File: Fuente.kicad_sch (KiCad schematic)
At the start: 0 parts

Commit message: Avance
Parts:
- added C1: 100nF/400VAC, Capacitor_THT:C_Disc_D10.5mm_W5.0mm_P7.50mm, symbol Device:C
- added C1, C6: 100nF/50v, 1-Capacitor:C_0805_2012Metric, symbol Device:C
- added C2: 220uF/25v, Capacitor_THT:CP_Radial_D8.0mm_P3.50mm, symbol Device:C_Polarized
- added C3, C4: 1uF/50v, 1-Capacitor:C_1206_3216Metric, symbol 1-Capacitor:C_1206
- added C38, C60: 10uF/16V, Capacitor_THT:CP_Radial_D5.0mm_P2.50mm, symbol Device:C_Polarized
- added C59, C61: 1uF 50V, 1-Capacitor:C_1206_3216Metric, symbol 1-Capacitor:C_0805
- added F1: 250VAC 0.5AAC, Fuse:Fuseholder_TR5_Littelfuse_No560_No460, symbol Device:Fuse
- added J8: Screw_Terminal_01x02, 1-Terminal-Block:DG126_5.0_02P, symbol 1-Terminal-Block:DG126_5.0_02P
- added PS2: IRM-10-24, Converter_ACDC:Converter_ACDC_MeanWell_IRM-10-xx_THT, symbol Converter_ACDC:IRM-10-24
- added RV1: 10D561K, Varistor:RV_Disc_D12mm_W3.9mm_P7.5mm, symbol Device:Varistor
- added U4, U6: LD29150, Package_TO_SOT_SMD:TO-252-2, symbol LIB_SCH_CONTR:LD29150
- added U5: L78M08CDT-TR, Package_TO_SOT_SMD:TO-252-2, symbol Regulator_Linear:uA7810
- added U7: OKI-78SR-12_1.0-W36-C, Converter_DCDC:Converter_DCDC_Murata_OKI-78SR_Vertical, symbol Converter_DCDC:OKI-78SR-12_1.0-W36-C
- added U8: uA7810, Package_TO_SOT_SMD:TO-263-3_TabPin2, symbol Regulator_Linear:uA7810
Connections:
- new net: F1.1, J8.1 (Pin_1)
- new net: C1.1, F1.2, PS2.2 (AC/L), RV1.1
- new net: C1.2, J8.2 (Pin_2), PS2.1 (AC/N), RV1.2
- new net 10V: C6.1, U8.3 (OUT)
- new net 12V: C3.1, C4.1, C59.1, U4.1 (IN), U5.1 (IN), U7.3 (OUT), U8.1 (IN)
- new net 24V: C2.1, PS2.4 (+Vo), U7.1 (IN)
- new net 3V3: C38.1, U6.3 (OUT)
- new net 5V: C60.1, C61.1, U4.3 (OUT), U6.1 (IN)
- new net 8V: C1.1, U5.3 (OUT)
- new net GND: C1.2, C2.2, C3.2, C38.2, C4.2, C59.2, C6.2, C60.2, C61.2, PS2.3 (-Vo), U4.2 (GND), U5.2 (GND), U6.2 (GND), U7.2 (GND), U8.2 (GND)
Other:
- note added: "ANALOG"
- note added: "C1848"
- note added: "C2974807"
- note added: "LD29150DT33R"
- note added: "LD29150DT50R"
- note added: "MCU"
- note added: "NAMUR"
- note added: "REF"
- note added: "RELAY"

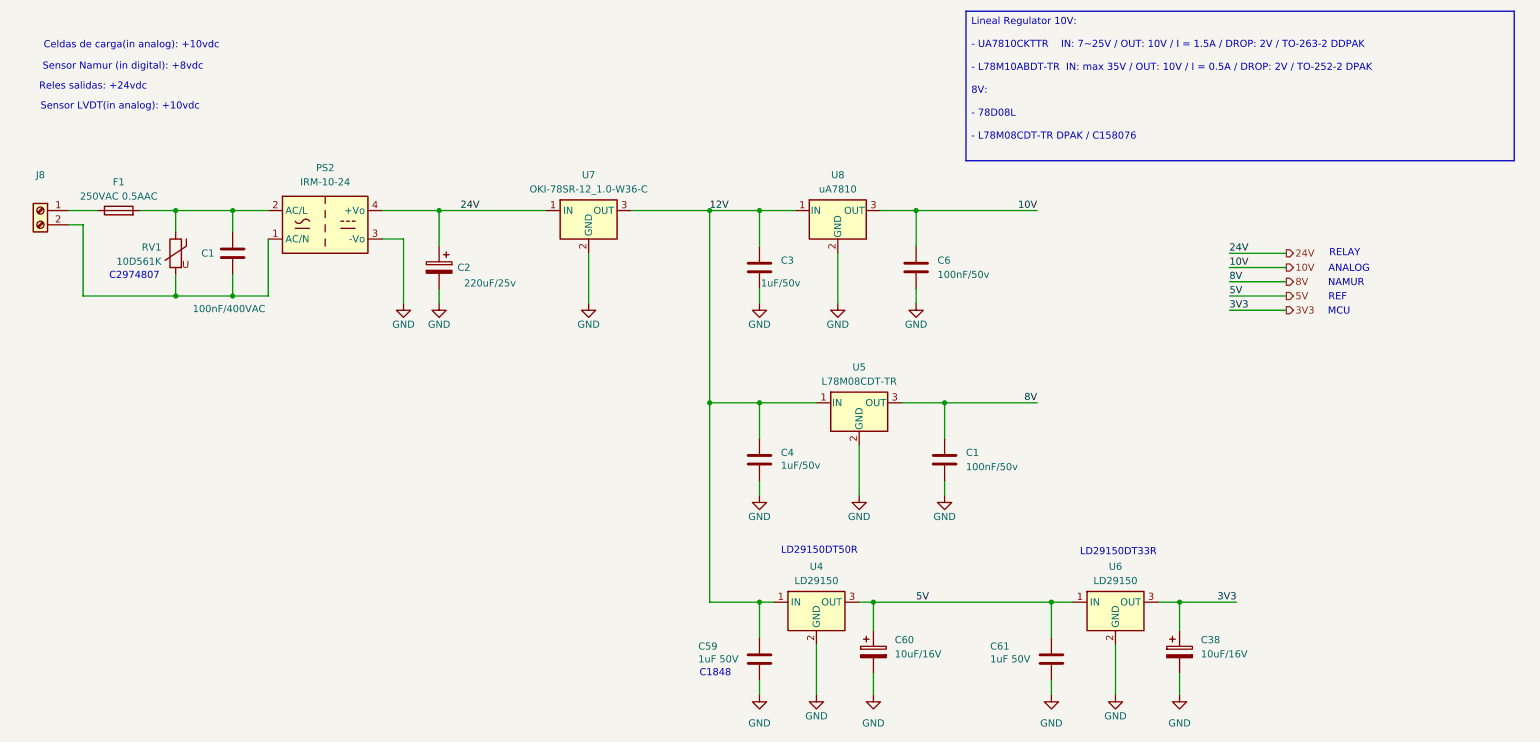
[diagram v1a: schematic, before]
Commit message: avance de pcb, se considera borneras externas para conexión de alimentación
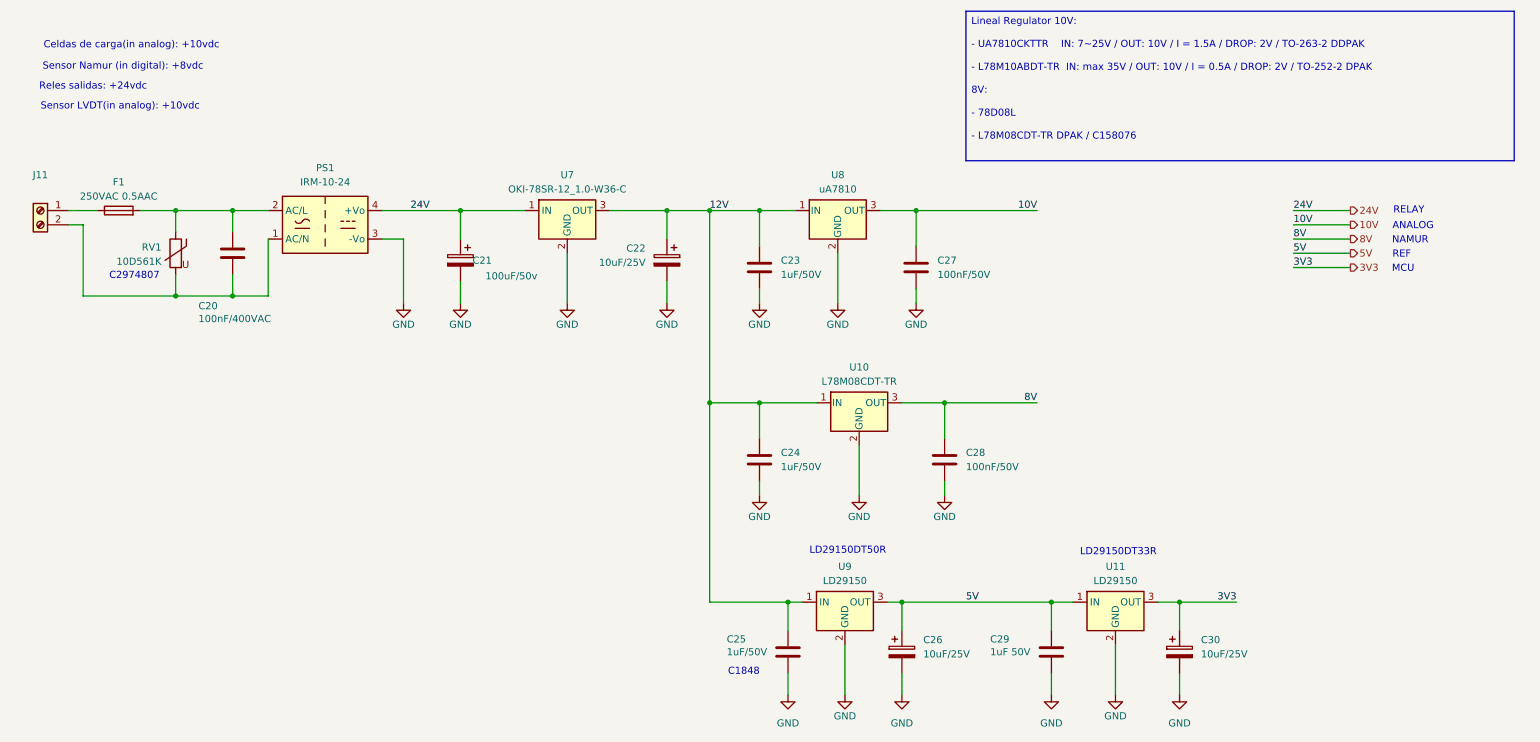
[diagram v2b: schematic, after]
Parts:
- removed C3, C4: 1uF/50v, 1-Capacitor:C_1206_3216Metric, symbol 1-Capacitor:C_1206
- added C22: 10uF/25V, Capacitor_THT:CP_Radial_D5.0mm_P2.50mm, symbol Device:C_Polarized
- added C23, C24: 1uF/50V, Capacitor_SMD:C_1206_3216Metric, symbol Device:C
- C21: renamed from C2; value 220uF/25v -> 100uF/50v; footprint Capacitor_THT:CP_Radial_D8.0mm_P3.50mm -> Capacitor_THT:CP_Radial_D10.0mm_P5.00mm
- C25: renamed from C59; value 1uF 50V -> 1uF/50V; footprint 1-Capacitor:C_1206_3216Metric -> Capacitor_SMD:C_1206_3216Metric
- C26: renamed from C60; value 10uF/16V -> 10uF/25V
- C27: renamed from C6; value 100nF/50v -> 100nF/50V; footprint 1-Capacitor:C_0805_2012Metric -> Capacitor_SMD:C_0603_1608Metric
- C28: renamed from C1; value 100nF/50v -> 100nF/50V; footprint 1-Capacitor:C_0805_2012Metric -> Capacitor_SMD:C_0603_1608Metric
- C29: renamed from C61; footprint 1-Capacitor:C_1206_3216Metric -> Capacitor_SMD:C_1206_3216Metric
- C30: renamed from C38; value 10uF/16V -> 10uF/25V
- renumbered C1 to C20, J8 to J11, PS2 to PS1, U5 to U10, U6 to U11, U4 to U9
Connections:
- net 12V: now also C22.1, C23.1, C24.1
- net GND: now also C22.2, C23.2, C24.2
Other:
- moved on the sheet: C21, C25, C26, C29, U7, U9

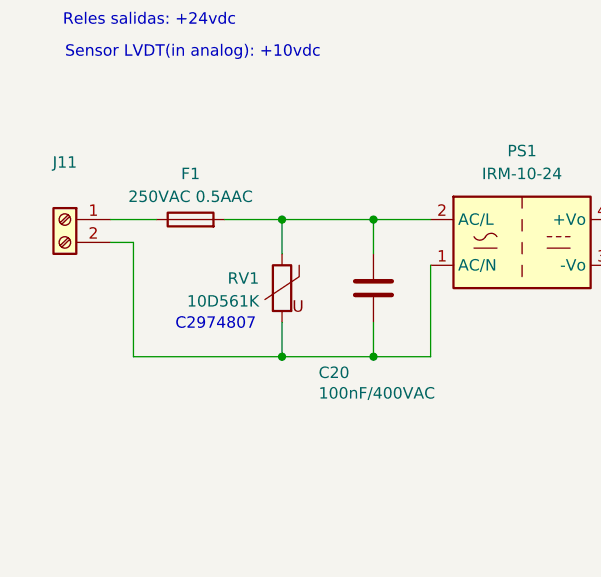
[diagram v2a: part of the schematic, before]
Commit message: Se traza vcc, digital, analog, relay, esta por terminar corregir GND y revisar nuevamente
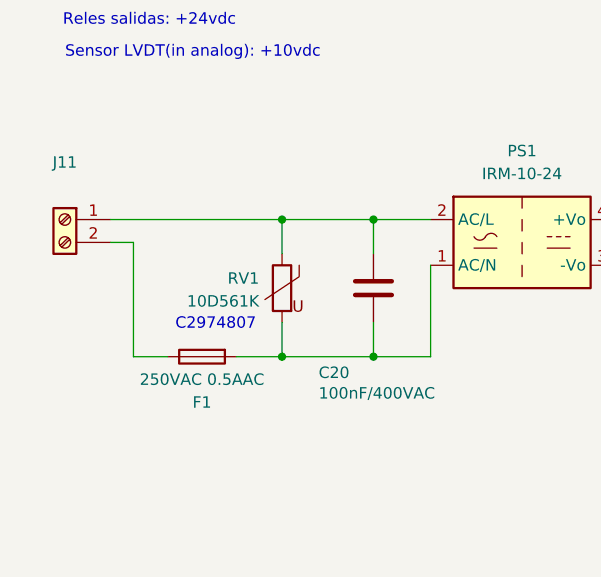
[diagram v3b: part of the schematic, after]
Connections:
- net at F1.1: now also J11.2 (Pin_2); no longer J11.1 (Pin_1)
- net at C20.1, PS1.2 (AC/L), RV1.1: now also J11.1 (Pin_1); no longer F1.2
- net at C20.2, PS1.1 (AC/N), RV1.2: now also F1.2; no longer J11.2 (Pin_2)
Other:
- moved on the sheet: F1
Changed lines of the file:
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@@
 	(wire
 		(pts
-			(xy 24.13 49.53) (xy 29.21 49.53)
+			(xy 24.13 49.53) (xy 43.18 49.53)
 		)
 		(stroke
@@
 	(wire
 		(pts
+			(xy 38.1 64.77) (xy 43.18 64.77)
+		)
+		(stroke
+			(width 0)
+			(type default)
+		)
+	)
+	(wire
+		(pts
 			(xy 120.65 49.53) (xy 130.81 49.53)
 		)
@@
 	(wire
 		(pts
-			(xy 26.67 64.77) (xy 43.18 64.77)
+			(xy 26.67 64.77) (xy 30.48 64.77)
 		)
 		(stroke
@@
 		(pts
 			(xy 152.4 119.38) (xy 152.4 124.46)
-		)
-		(stroke
-			(width 0)
-			(type default)
-		)
-	)
-	(wire
-		(pts
-			(xy 36.83 49.53) (xy 43.18 49.53)
 		)
 		(stroke
@@
 	(symbol
 		(lib_id "Device:Fuse")
-		(at 33.02 49.53 90)
+		(at 34.29 64.77 90)
+		(mirror x)
 		(unit 1)
 		(exclude_from_sim no)
@@
 		(on_board yes)
 		(dnp no)
-		(fields_autoplaced yes)
 		(property "Reference" "F1"
-			(at 33.02 44.45 90)
+			(at 34.29 69.85 90)
 			(effects
 				(font
@@
 		)
 		(property "Value" "250VAC 0.5AAC"
-			(at 33.02 46.99 90)
+			(at 34.29 67.31 90)
 			(effects
 				(font
@@
 		)
 		(property "Footprint" "Fuse:Fuseholder_TR5_Littelfuse_No560_No460"
-			(at 33.02 51.308 90)
+			(at 34.29 62.992 90)
 			(effects
 				(font
@@
 		)
 		(property "Datasheet" "~"
-			(at 33.02 49.53 0)
+			(at 34.29 64.77 0)
 			(effects
 				(font
@@
 		)
 		(property "Description" ""
-			(at 33.02 49.53 0)
+			(at 34.29 64.77 0)
 			(effects
 				(font

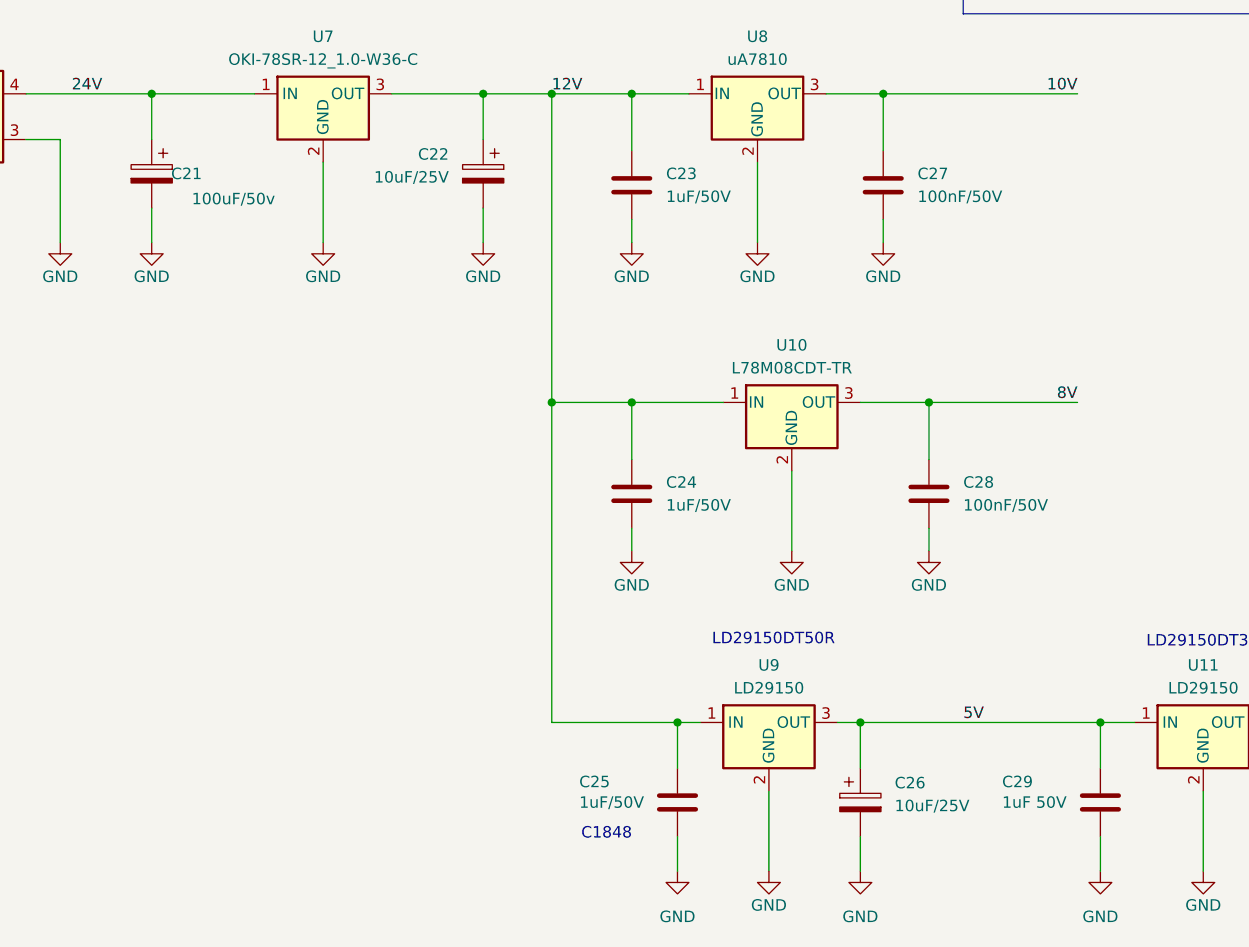
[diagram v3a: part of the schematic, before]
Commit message: Se añaden leds a la entrada de los Namur. Se estandariza y revisan varios footprints de los capacitores. El cambio no fue demasiado, se corrigio en placa. Se hacen algunos cambios adicionales a los valores. Se realiza un avance para jlcpcb
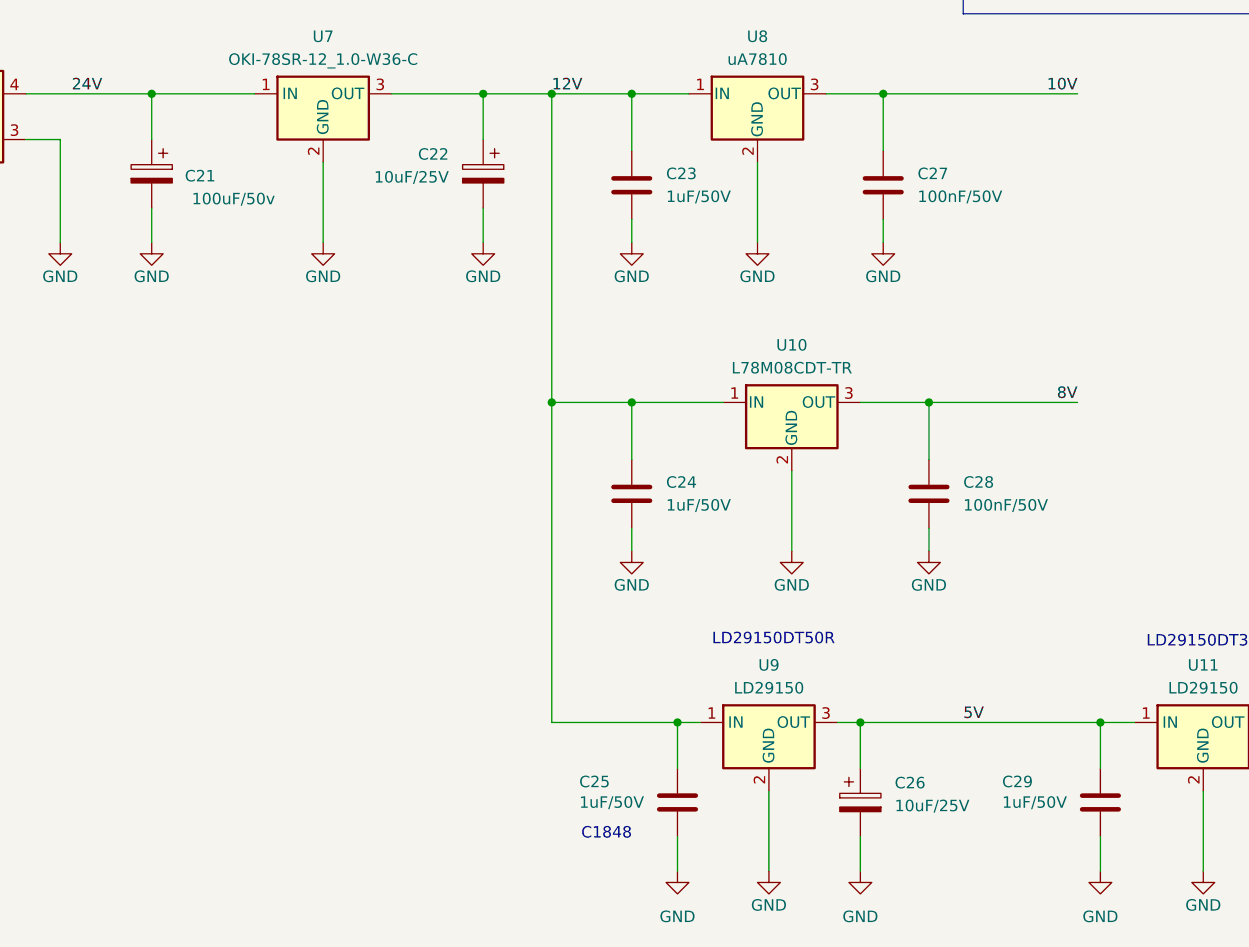
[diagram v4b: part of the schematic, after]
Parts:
- C29: value 1uF 50V -> 1uF/50V
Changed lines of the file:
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@@
 			)
 		)
-		(property "Value" "1uF 50V"
+		(property "Value" "1uF/50V"
 			(at 188.468 128.27 0)
 			(effects
@@
 		(dnp no)
 		(property "Reference" "C21"
-			(at 99.568 58.42 0)
+			(at 101.092 58.674 0)
 			(effects
 				(font

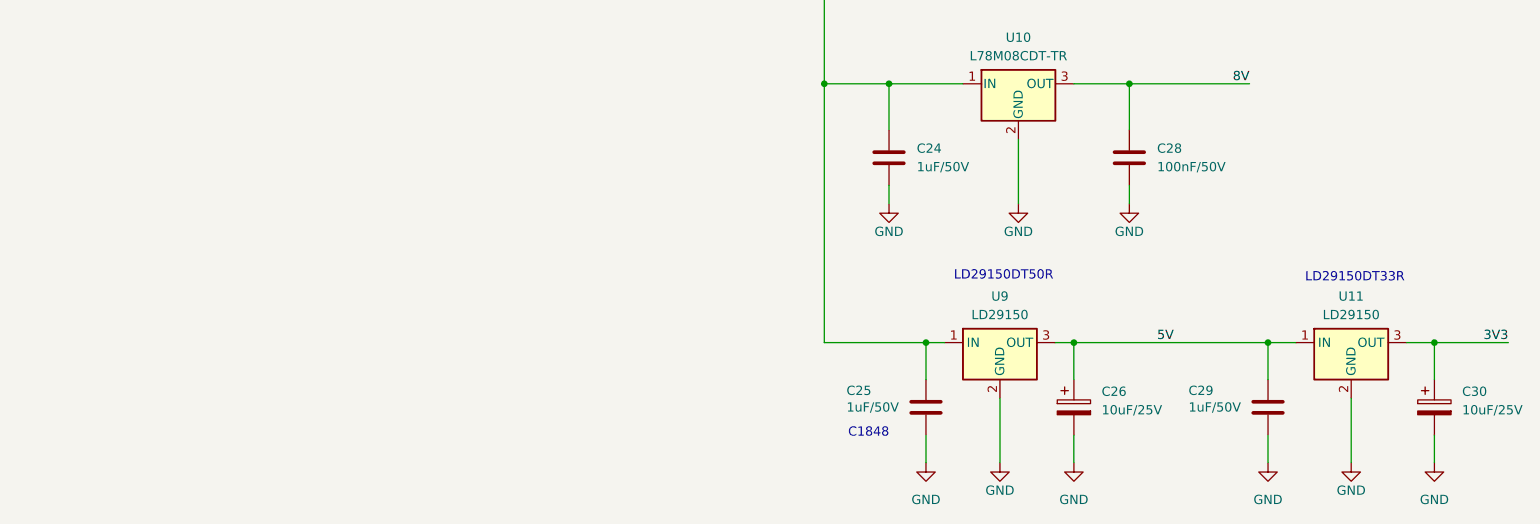
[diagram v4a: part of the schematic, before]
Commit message: Se añade led de status y eeprom externa. Se actualiza pcb y se añade serigrafía adicional. Se actualiza los componentes jlcpcb, se utiliza un micro con con 512kbytes de flash a recomendacion de jefry debido a la escasez de los de 1024 kbytes. Se revisa y se espera mandar a china
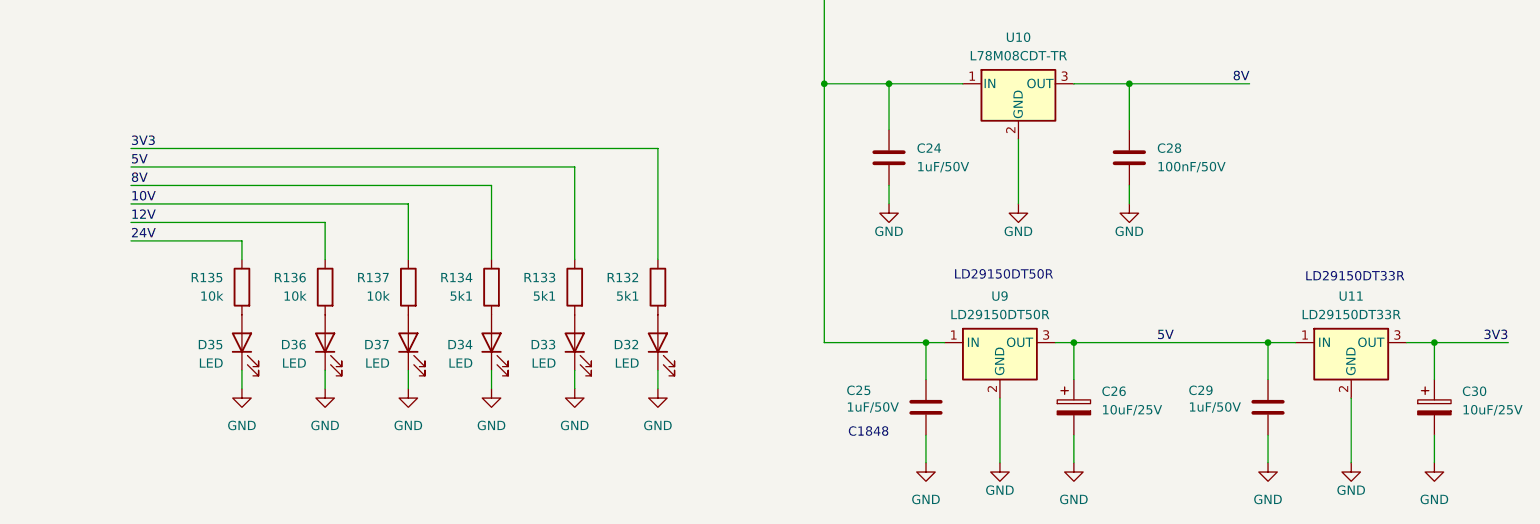
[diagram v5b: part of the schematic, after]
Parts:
- added D32, D33, D34, D35, D36, D37: LED, LED_SMD:LED_0805_2012Metric, symbol Device:LED
- added R132, R133, R134: 5k1, Resistor_SMD:R_0603_1608Metric, symbol Device:R
- added R135, R136, R137: 10k, Resistor_SMD:R_0603_1608Metric, symbol Device:R
- U11: value LD29150 -> LD29150DT33R
- U9: value LD29150 -> LD29150DT50R
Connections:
- net 10V: now also R137.1
- net 12V: now also R136.1
- net 24V: now also R135.1
- net 3V3: now also R132.1
- net 5V: now also R133.1
- net 8V: now also R134.1
- net GND: now also D32.1 (K), D33.1 (K), D34.1 (K), D35.1 (K), D36.1 (K), D37.1 (K)
- new net: D33.2 (A), R133.2
- new net: D36.2 (A), R136.2
- new net: D32.2 (A), R132.2
- new net: D37.2 (A), R137.2
- new net: D35.2 (A), R135.2
- new net: D34.2 (A), R134.2
